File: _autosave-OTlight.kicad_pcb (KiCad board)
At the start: 2 copper layers, 90 x 55 mm, 78 parts, among them P1 CONN_01X01, Q1 TEMT6000, Q2 Q_NMOS_GSD, T1 TRANSFO, U1 LM3478, U10 IN-14, U11 IN-14, U12 MAX6931, U13 IN-14, U14 MAX6920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

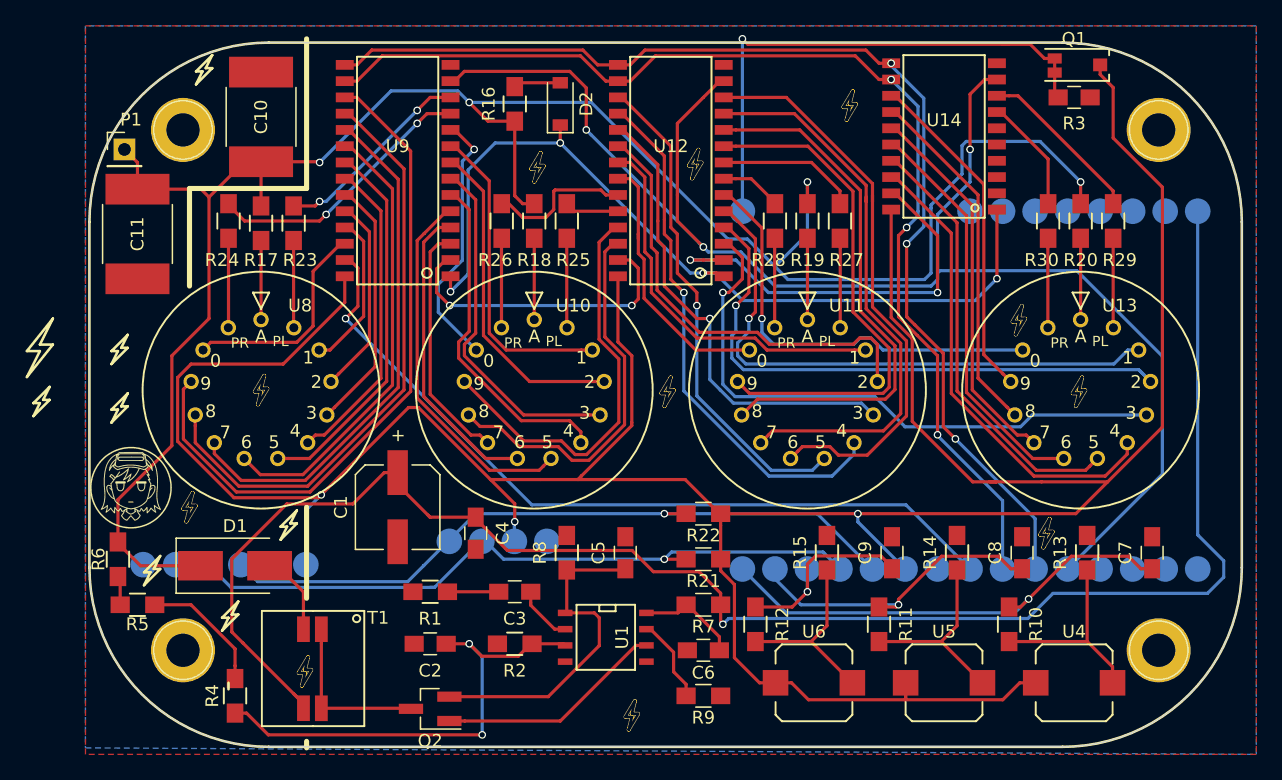
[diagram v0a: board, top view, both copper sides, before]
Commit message: Board size to fit Altoids+ decoupling caps
NOTHING IS WHERE IT SHOULD BE
EVERYTHING IS WRONG
I AM GOING TO BED!
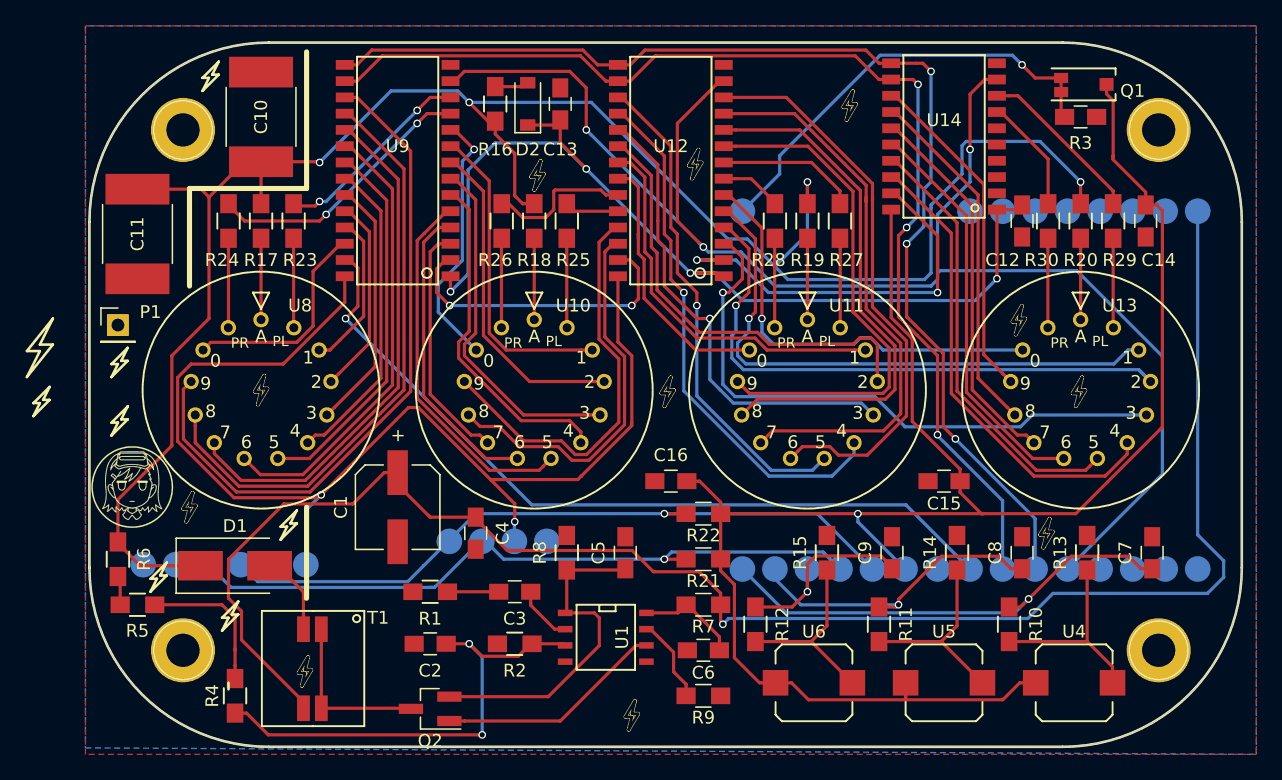
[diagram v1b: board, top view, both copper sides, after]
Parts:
- added C12: C_Small, Capacitors_SMD:C_0805_HandSoldering, F.Cu at (116.8, 90.9)
- added C13: C_Small, Capacitors_SMD:C_0805_HandSoldering, F.Cu at (80.8, 81.8)
- added C14: C_Small, Capacitors_SMD:C_0805_HandSoldering, F.Cu at (126.5, 90.9)
- added C15: C_Small, Capacitors_SMD:C_0805_HandSoldering, F.Cu at (110.7, 111.3)
- added C16: C_Small, Capacitors_SMD:C_0805_HandSoldering, F.Cu at (89.4, 111.3)
- moved P1 13.7 mm to (46.2, 99.1)
- moved D2 2.54 mm to (78.2, 81.8)
- moved R3 1.61 mm to (121.4, 82.8)
- moved Q1 1.60 mm to (119.9, 80.3)
- moved R16 1.52 mm to (75.7, 81.8)
- moved REF** 0.64 mm to (79.0, 87.4)
- moved R17 0.17 mm to (57.4, 90.9)
- moved R23 0.17 mm to (59.9, 90.9)
- moved G*** 0.11 mm to (47.3, 111.7)
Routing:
- net +3V3: track 252.2 -> 235.1 mm
- net Net-(C12-Pad2): track 67.7 -> 76.9 mm
- net Net-(Q1-Pad2): track 42.1 -> 34.7 mm
- net /HVout: track 160.8 -> 156.4 mm
- net /CLK: track 90.1 -> 92.0 mm
- net Net-(R4-Pad1): track 10.0 -> 11.6 mm
- net Net-(D2-Pad2): track 3.68 -> 2.66 mm
- net Net-(U12-Pad2): track 32.7 -> 31.7 mm
- net /LOAD: track 89.0 -> 90.0 mm
